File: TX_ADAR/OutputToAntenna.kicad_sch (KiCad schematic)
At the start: 12 parts, among them J10 Conn_Coaxial, J3 Conn_Coaxial, J4 Conn_Coaxial, J5 Conn_Coaxial, J6 Conn_Coaxial, J7 Conn_Coaxial, J8 Conn_Coaxial, J9 Conn_Coaxial

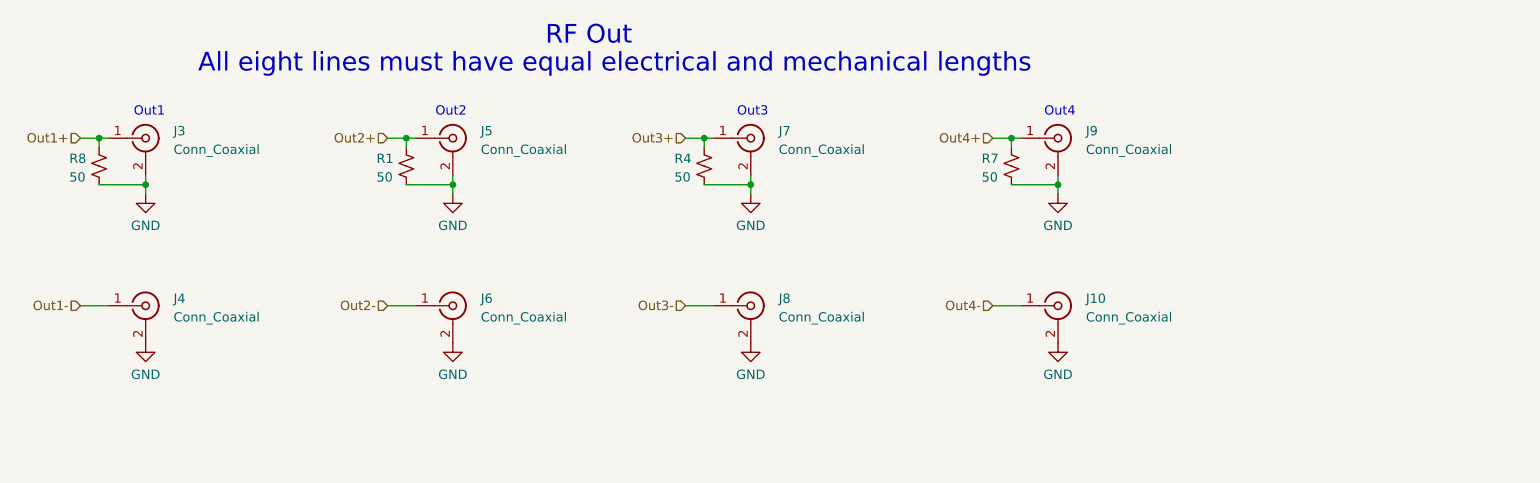
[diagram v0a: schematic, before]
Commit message: Fixed tracks & added images to schem
NEED: Find 50 ohm impedance width for OSH Park
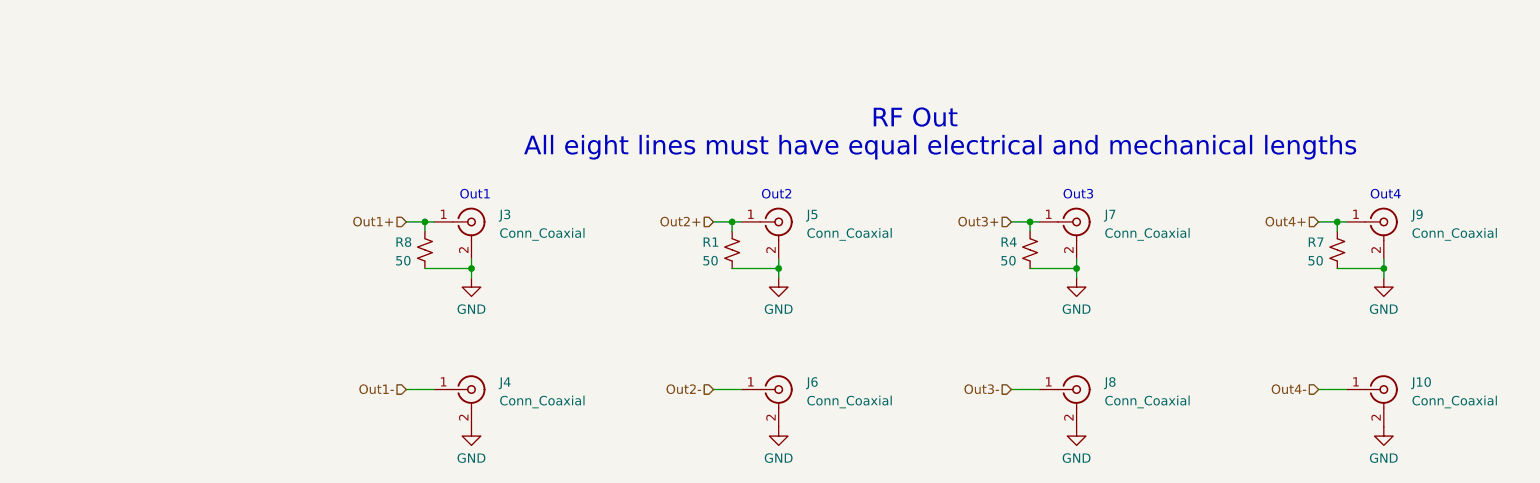
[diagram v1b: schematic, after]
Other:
- moved on the sheet: J10, J3, J4, J5, J6, J7, J8, J9, R1, R4, R7, R8
